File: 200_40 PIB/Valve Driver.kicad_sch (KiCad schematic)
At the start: 6 parts, among them J12 532610671, Q5 NMOS, U12 DRV8220DRL, U13 DRV8220DRL

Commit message: john.
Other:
- note added: "look into what was done on femta for NC valve"
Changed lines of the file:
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@@
+		)
+	)
+	(text "look into what was done on femta for NC valve"
+		(exclude_from_sim no)
+		(at 185.42 90.424 0)
+		(effects
+			(font
+				(size 1.27 1.27)
+			)
 		)
 	)

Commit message: .nhoj
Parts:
- removed Q5: NMOS, symbol Simulation_SPICE:NMOS
- removed U12, U13: DRV8220DRL, Package_TO_SOT_SMD:SOT-563, symbol Driver_Motor:DRV8220DRL
- added C7, C8: 10uF, Capacitor_SMD:C_0805_2012Metric, symbol Device:C
- added Q10: IRF7832, Package_SO:SOIC-8_3.9x4.9mm_P1.27mm, symbol Transistor_FET:IRF7403
- added U2, U3: MIC4424YM, Package_SO:SOIC-8_3.9x4.9mm_P1.27mm, symbol MIC4424YM:MIC4424YM
- R6: value 100k -> 100K
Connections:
- net +12V: now also C7.1, C8.1, U2.6 (VS), U3.6 (VS)
- net LHL1: now also U2.2 (INA)
- net LHL2: now also U2.4 (INB)
- net LHL3: now also U3.2 (INA)
- net LHL4: now also U3.4 (INB)
- net at J12.6: now also Q10.5 (D), Q10.6 (D), Q10.7 (D), Q10.8 (D)
- net at R5.2: now also Q10.4 (G)
- net at J12.1: now also U2.7 (OUTA)
- net at J12.2: now also U2.5 (OUTB)
- net at J12.3: now also U3.7 (OUTA)
- net at J12.4: now also U3.5 (OUTB)
- net GNDPWR renamed GND
- net GND: now also C7.2, C8.2, Q10.1 (S), Q10.2 (S), Q10.3 (S), U2.3 (GND), U3.3 (GND)
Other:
- moved on the sheet: R6

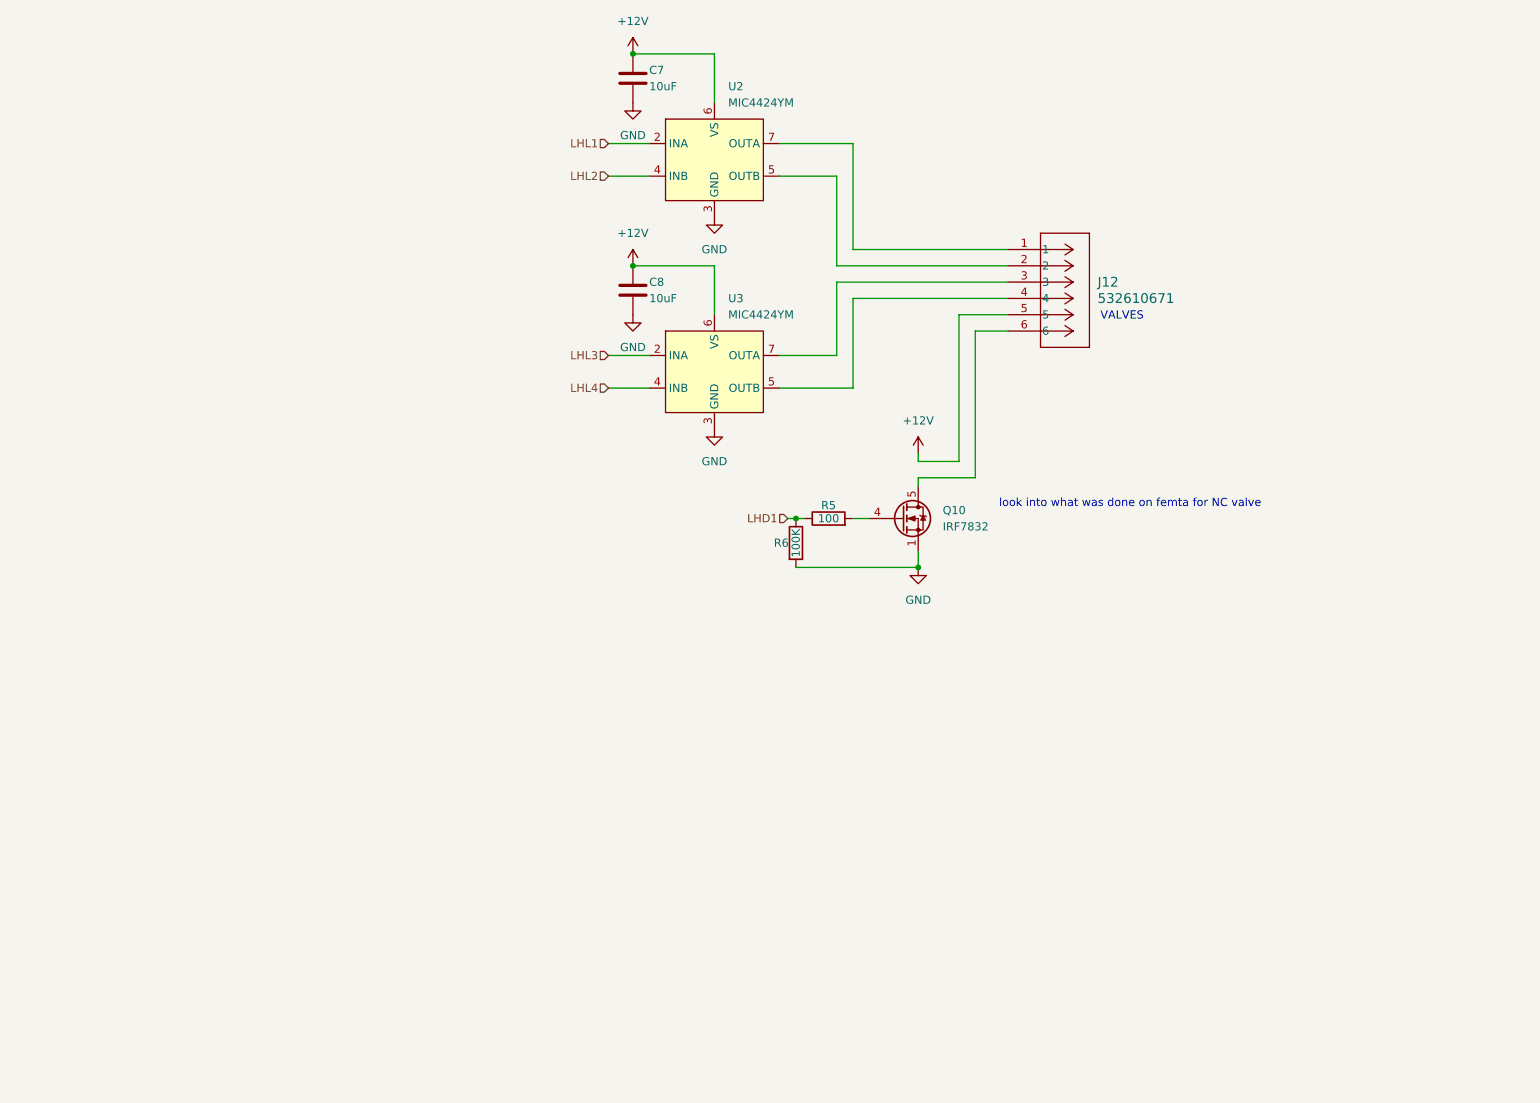
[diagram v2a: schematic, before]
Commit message: switch to G431RB and assign pins
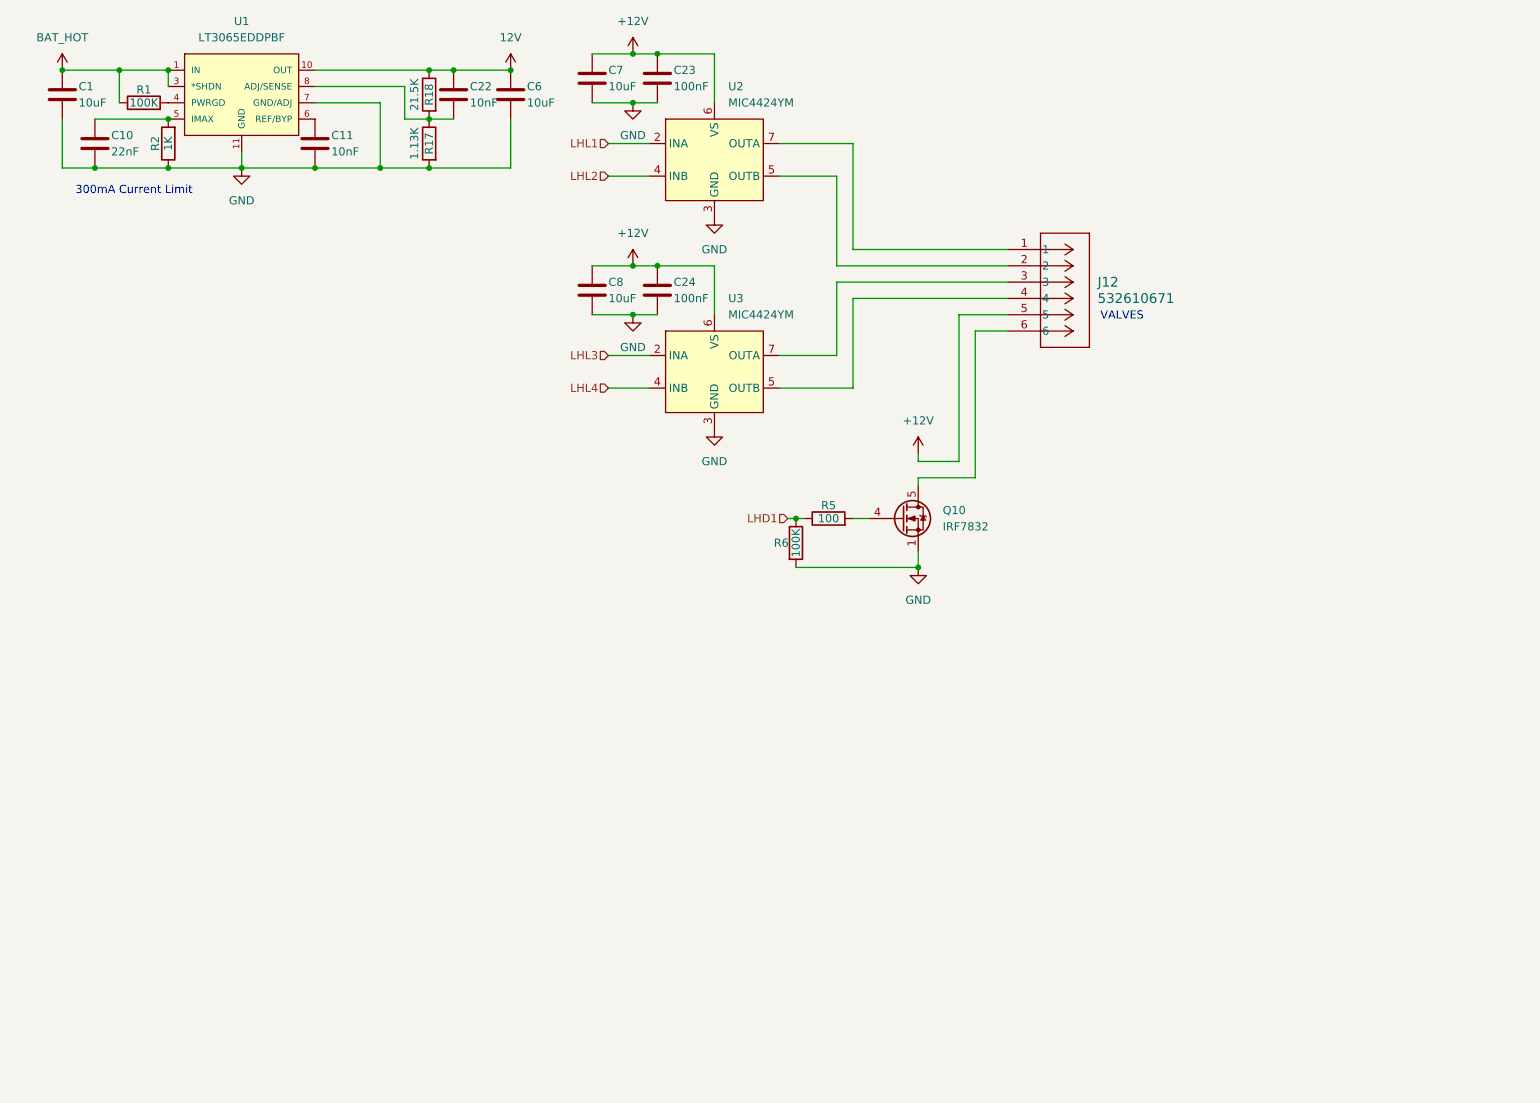
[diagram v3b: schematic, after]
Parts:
- added C1, C6: 10uF, Capacitor_SMD:C_0805_2012Metric, symbol Device:C
- added C10: 22nF, Capacitor_SMD:C_0603_1608Metric, symbol Device:C
- added C11: 10nF, Capacitor_SMD:C_0603_1608Metric, symbol Device:C
- added C22: 10nF, Capacitor_SMD:C_0402_1005Metric, symbol Device:C
- added C23, C24: 100nF, Capacitor_SMD:C_0402_1005Metric, symbol Device:C
- added R1: 100K, Resistor_SMD:R_0402_1005Metric, symbol Device:R
- added R17: 1.13K, Resistor_SMD:R_0402_1005Metric, symbol Device:R
- added R18: 21.5K, Resistor_SMD:R_0402_1005Metric, symbol Device:R
- added R2: 1K, Resistor_SMD:R_0402_1005Metric, symbol Device:R
- added U1: LT3065EDDPBF, 0_PAY_Footprint_Library:DFN-10_DD, symbol LT3065EDDPBF:LT3065EDDPBF
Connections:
- net +12V: now also C23.1, C24.1
- net GND: now also C1.2, C10.2, C11.2, C23.2, C24.2, C6.2, R17.2, R2.1, U1.11 (GND), U1.7 (GND/ADJ)
- new net: C22.2, R17.1, R18.2, U1.8 (ADJ/SENSE)
- new net: C10.1, R2.2, U1.5 (IMAX)
- new net: R1.2, U1.4 (PWRGD)
- new net: C11.1, U1.6 (REF/BYP)
- new net 12V: C22.1, C6.1, R18.1, U1.10 (OUT), U1.9 (OUT)
- new net BAT_HOT: C1.1, R1.1, U1.1 (IN), U1.2 (IN), U1.3 (*SHDN)
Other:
- note added: "300mA Current Limit"
- note removed: "look into what was done on femta for NC valve"
- moved on the sheet: C7, C8

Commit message: pib work
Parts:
- removed J12: 532610671, CONN_532610001-SD_06_MOL, symbol 0_PAY_Symbol_Library:532610671
- added C2, C3: 10uF, Capacitor_SMD:C_0805_2012Metric, symbol Device:C
- added C31: 100nF, Capacitor_SMD:C_0402_1005Metric, symbol Device:C
- added J4: 53261-0671, Connector_Molex:Molex_PicoBlade_53261-0671_1x06-1MP_P1.25mm_Horizontal, symbol Connector:Conn_01x06_Pin
- added R10, R11, R12, R38, R43, R47: 1K, Resistor_SMD:R_0402_1005Metric, symbol Device:R
- added R39, R40, R41, R42, R44: 100K, symbol Device:R
- added R45: 10K, Capacitor_SMD:C_0603_1608Metric, symbol Device:R
- added R46: 43K, Capacitor_SMD:C_0603_1608Metric, symbol Device:R
- added U6: LM1117MP-3.3, Package_TO_SOT_SMD:SOT-223-3_TabPin2, symbol Regulator_Linear:LM1117MP-3.3
- added U8: 74LVC1GU04DRL, Package_TO_SOT_SMD:SOT-553, symbol 74xGxx:74LVC1GU04DRL
- added U9: 74LVC2G126DCU, symbol 74xGxx:74LVC2G126
- R5: value 100 -> 1K
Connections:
- net +12V: now also J4.5 (Pin_5)
- net GND: now also C2.2, C3.2, C31.2, R39.2, R40.2, R41.2, R42.2, R44.2, R45.1, U6.1 (GND), U8.3 (GND), U9.4 (GND)
- net LHD1: no longer R6.1
- net LHL1: now also R12.1; no longer U2.2 (INA)
- net LHL2: now also R38.1; no longer U2.4 (INB)
- net LHL3: now also R10.1; no longer U3.2 (INA)
- net LHL4: now also R11.1; no longer U3.4 (INB)
- net at U2.7 (OUTA): now also J4.1 (Pin_1)
- net at U2.5 (OUTB): now also J4.2 (Pin_2)
- net at U3.7 (OUTA): now also J4.3 (Pin_3)
- net at U3.5 (OUTB): now also J4.4 (Pin_4)
- net at Q10.5 (D), Q10.6 (D), Q10.7 (D)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: now also J4.6 (Pin_6)
- net at Q10.4 (G), R5.2: now also R6.1, R47.2
- new net: R10.2, R42.1, U3.2 (INA), U9.3
- new net: U8.4, U9.5
- new net: R45.2, R46.1, U9.1, U9.7
- new net: R12.2, R40.1, U2.2 (INA)
- new net: R43.2, R44.1, U8.2, U9.2
- new net: R11.2, R41.1, U3.4 (INB), U9.6
- new net: R38.2, R39.1, U2.4 (INB)
- new net 12V_GSE: C2.1, R46.2, U6.3 (VI)
- new net 3.3V_EGSE: C3.1, C31.1, U6.2 (VO), U8.5 (VCC), U9.8 (VCC)
- new net EGSE_OPEN: R43.1, R47.1
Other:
- note added: "Rough "UVLO" feature"
- note added: "Tristate buffer ensures backdrive is not an issue"
- moved on the sheet: C23, C24, C7, C8, Q10, R5, R6, U2, U3

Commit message: assign PIB footprints, push ioc file to CubeMX 6.18.1
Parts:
- C22, C23, C24, C31: footprint Capacitor_SMD:C_0402_1005Metric -> Capacitor_SMD:C_0603_1608Metric
- R1, R10, R11, R12, R17, R18, R2, R38, R43, R47: footprint Resistor_SMD:R_0402_1005Metric -> Resistor_SMD:R_0603_1608Metric
- R39, R40, R41, R42, R44, R5, R6: footprint (none) -> Resistor_SMD:R_0603_1608Metric
- R45, R46: footprint Capacitor_SMD:C_0603_1608Metric -> Resistor_SMD:R_0603_1608Metric
- U9: footprint (none) -> Package_SO:VSSOP-8_2.3x2mm_P0.5mm
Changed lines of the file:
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@@
 			)
 		)
-		(property "Footprint" ""
+		(property "Footprint" "Package_SO:VSSOP-8_2.3x2mm_P0.5mm"
 			(at 91.44 134.62 0)
 			(hide yes)
@@
 			)
 		)
-		(property "Footprint" "Resistor_SMD:R_0402_1005Metric"
+		(property "Footprint" "Resistor_SMD:R_0603_1608Metric"
 			(at 77.978 34.29 90)
 			(hide yes)
@@
 			)
 		)
-		(property "Footprint" "Resistor_SMD:R_0402_1005Metric"
+		(property "Footprint" "Resistor_SMD:R_0603_1608Metric"
 			(at 186.69 118.618 90)
 			(hide yes)
@@
 			)
 		)
-		(property "Footprint" "Resistor_SMD:R_0402_1005Metric"
+		(property "Footprint" "Resistor_SMD:R_0603_1608Metric"
 			(at 37.338 34.29 90)
 			(hide yes)
@@
 			)
 		)
-		(property "Footprint" "Resistor_SMD:R_0402_1005Metric"
+		(property "Footprint" "Resistor_SMD:R_0603_1608Metric"
 			(at 31.75 29.718 90)
 			(hide yes)
@@
 			)
 		)
-		(property "Footprint" ""
+		(property "Footprint" "Resistor_SMD:R_0603_1608Metric"
 			(at 154.432 62.23 90)
 			(hide yes)
@@
 			)
 		)
-		(property "Footprint" ""
+		(property "Footprint" "Package_SO:VSSOP-8_2.3x2mm_P0.5mm"
 			(at 76.2 165.1 0)
 			(hide yes)
@@
 			)
 		)
-		(property "Footprint" "Resistor_SMD:R_0402_1005Metric"
+		(property "Footprint" "Resistor_SMD:R_0603_1608Metric"
 			(at 41.91 136.398 90)
 			(hide yes)
@@
 			)
 		)
-		(property "Footprint" "Resistor_SMD:R_0402_1005Metric"
+		(property "Footprint" "Resistor_SMD:R_0603_1608Metric"
 			(at 148.59 52.578 90)
 			(hide yes)
@@
 			)
 		)
-		(property "Footprint" ""
+		(property "Footprint" "Resistor_SMD:R_0603_1608Metric"
 			(at 186.69 110.998 90)
 			(hide yes)
@@
 			)
 		)
-		(property "Footprint" "Capacitor_SMD:C_0402_1005Metric"
+		(property "Footprint" "Capacitor_SMD:C_0603_1608Metric"
 			(at 80.9752 30.48 0)
 			(hide yes)
@@
 			)
 		)
-		(property "Footprint" "Capacitor_SMD:C_0402_1005Metric"
+		(property "Footprint" "Capacitor_SMD:C_0603_1608Metric"
 			(at 172.4152 44.45 0)
 			(hide yes)
@@
 			)
 		)
-		(property "Footprint" ""
+		(property "Footprint" "Package_SO:VSSOP-8_2.3x2mm_P0.5mm"
 			(at 91.44 114.3 0)
 			(hide yes)
@@
 			)
 		)
-		(property "Footprint" ""
+		(property "Footprint" "Resistor_SMD:R_0603_1608Metric"
 			(at 150.622 62.23 90)
 			(hide yes)
@@
 			)
 		)
-		(property "Footprint" "Resistor_SMD:R_0402_1005Metric"
+		(property "Footprint" "Resistor_SMD:R_0603_1608Metric"
 			(at 101.6 85.598 90)
 			(hide yes)
@@
 			)
 		)
-		(property "Footprint" ""
+		(property "Footprint" "Resistor_SMD:R_0603_1608Metric"
 			(at 103.632 95.25 90)
 			(hide yes)
@@
 			)
 		)
-		(property "Footprint" "Resistor_SMD:R_0402_1005Metric"
+		(property "Footprint" "Resistor_SMD:R_0603_1608Metric"
 			(at 101.6 90.678 90)
 			(hide yes)
@@
 			)
 		)
-		(property "Footprint" "Capacitor_SMD:C_0402_1005Metric"
+		(property "Footprint" "Capacitor_SMD:C_0603_1608Metric"
 			(at 172.4152 77.47 0)
 			(hide yes)
@@
 			)
 		)
-		(property "Footprint" "Resistor_SMD:R_0402_1005Metric"
+		(property "Footprint" "Resistor_SMD:R_0603_1608Metric"
 			(at 148.59 57.658 90)
 			(hide yes)
@@
 			)
 		)
-		(property "Footprint" "Capacitor_SMD:C_0603_1608Metric"
+		(property "Footprint" "Resistor_SMD:R_0603_1608Metric"
 			(at 19.558 111.76 90)
 			(hide yes)
@@
 			)
 		)
-		(property "Footprint" ""
+		(property "Footprint" "Resistor_SMD:R_0603_1608Metric"
 			(at 107.442 95.25 90)
 			(hide yes)
@@
 			)
 		)
-		(property "Footprint" ""
+		(property "Footprint" "Resistor_SMD:R_0603_1608Metric"
 			(at 43.942 138.43 90)
 			(hide yes)
@@
 			)
 		)
-		(property "Footprint" "Capacitor_SMD:C_0603_1608Metric"
+		(property "Footprint" "Resistor_SMD:R_0603_1608Metric"
 			(at 19.558 119.38 90)
 			(hide yes)
@@
 			)
 		)
-		(property "Footprint" ""
+		(property "Footprint" "Resistor_SMD:R_0603_1608Metric"
 			(at 202.692 113.03 90)
 			(hide yes)
@@
 			)
 		)
-		(property "Footprint" "Capacitor_SMD:C_0402_1005Metric"
+		(property "Footprint" "Capacitor_SMD:C_0603_1608Metric"
 			(at 63.1952 168.91 0)
 			(hide yes)
@@
 			)
 		)
-		(property "Footprint" "Resistor_SMD:R_0402_1005Metric"
+		(property "Footprint" "Resistor_SMD:R_0603_1608Metric"
 			(at 77.978 26.67 90)
 			(hide yes)

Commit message: prelim layout for pib mainboard v1. TODO review
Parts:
- C10, C11, C22, C23, C24, C31: footprint Capacitor_SMD:C_0603_1608Metric -> Capacitor_SMD:C_0402_1005Metric
- J4: value 53261-0671 -> 53398-0671; footprint Connector_Molex:Molex_PicoBlade_53261-0671_1x06-1MP_P1.25mm_Horizontal -> Connector_Molex:Molex_PicoBlade_53398-0671_1x06-1MP_P1.25mm_Vertical
- R1, R10, R11, R12, R17, R18, R2, R38, R39, R40, R41, R42, R43, R44, R47, R5, R6: footprint Resistor_SMD:R_0603_1608Metric -> Resistor_SMD:R_0402_1005Metric
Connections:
- net 12V is gone; now on net +12V: C22.1, C6.1, R18.1, U1.10 (OUT), U1.9 (OUT)
- net at J4.1 (Pin_1): now also U2.5 (OUTB); no longer U2.7 (OUTA)
- net at J4.2 (Pin_2): now also U2.7 (OUTA); no longer U2.5 (OUTB)
- net at J4.3 (Pin_3): now also U3.5 (OUTB); no longer U3.7 (OUTA)
- net at J4.4 (Pin_4): now also U3.7 (OUTA); no longer U3.5 (OUTB)
